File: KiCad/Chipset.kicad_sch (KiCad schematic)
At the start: 9 parts, among them U2 OPTi_82C895, U3 OPTi_82C602, Y1 32768Hz

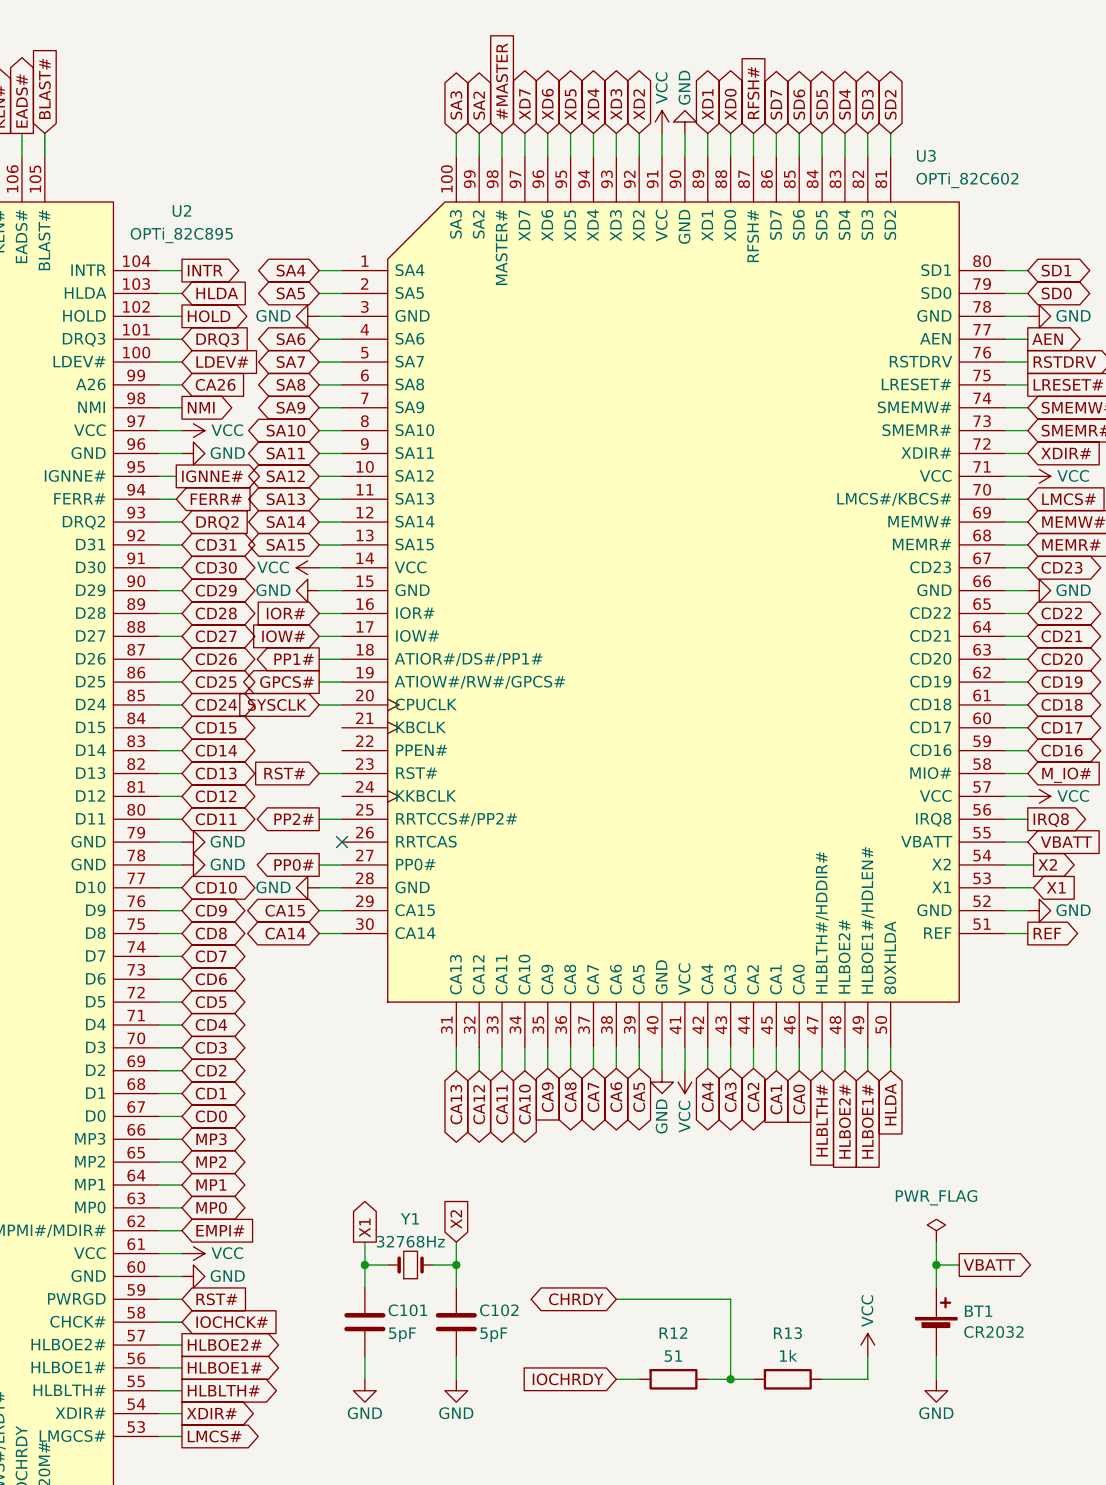
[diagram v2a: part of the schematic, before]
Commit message: Version 0.4: Update chipset connection
Signed-off-by: Sergey Kiselev <skiselev@gmail.com>
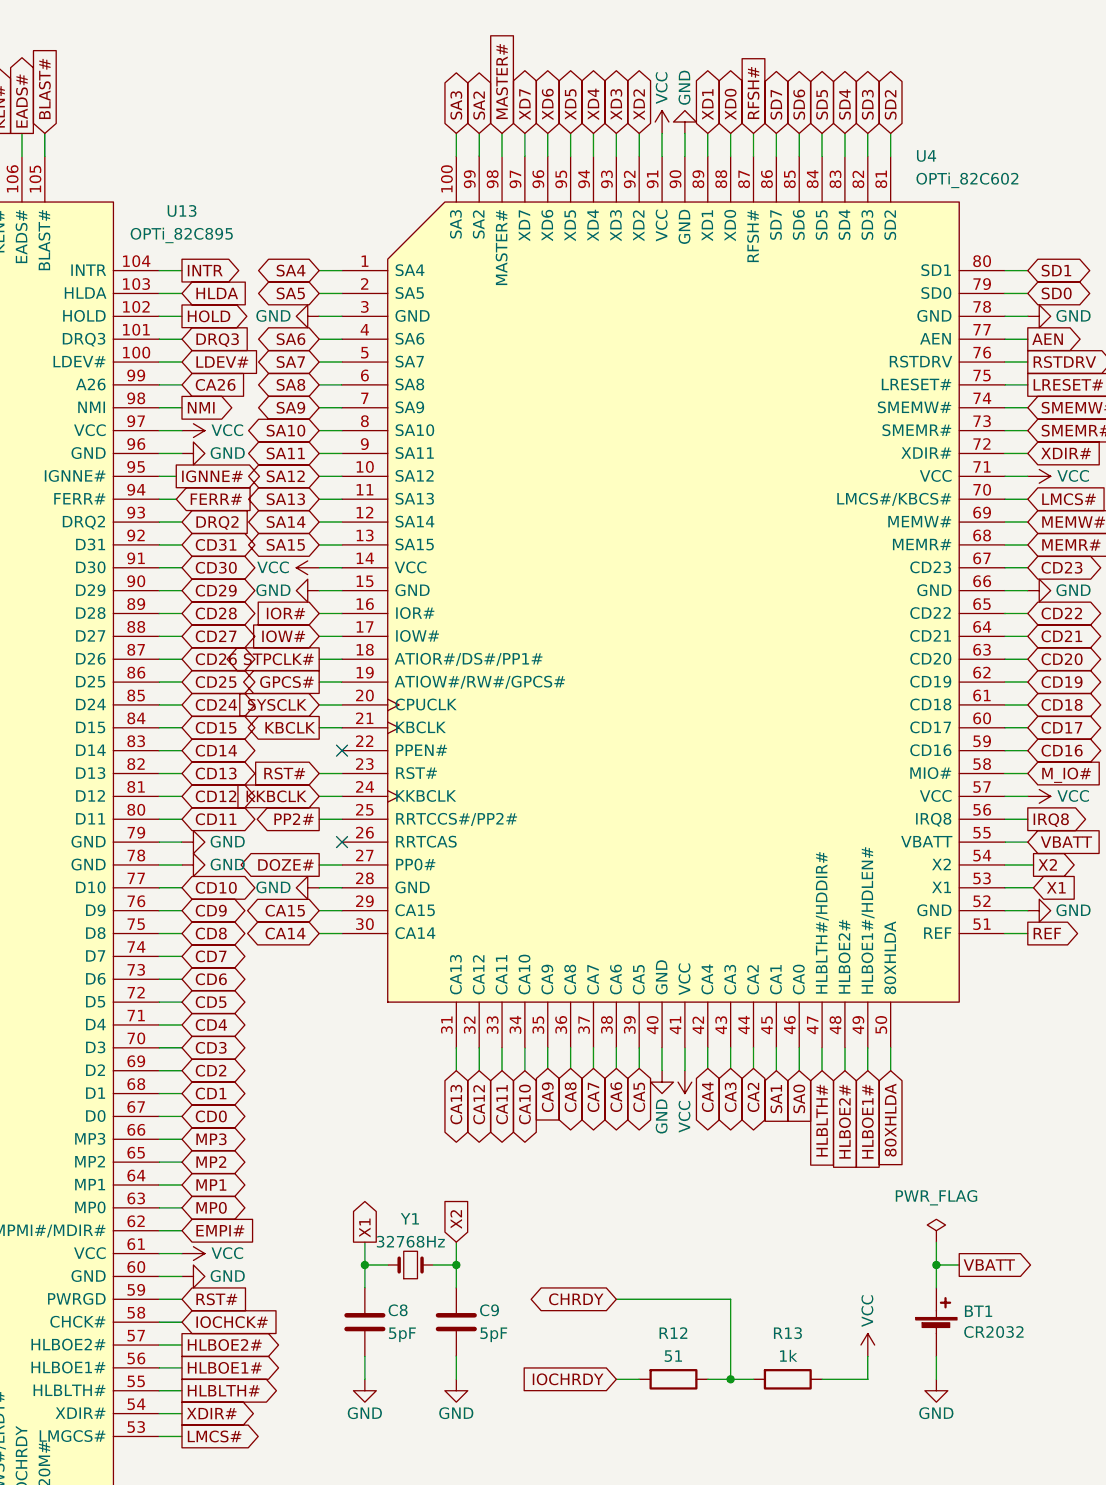
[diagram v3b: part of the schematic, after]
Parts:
- BT1: footprint (none) -> My_Components:Battery_Holder_CR2032_Universal
- C8: renamed from C101; footprint (none) -> Capacitor_SMD:C_0603_1608Metric_Pad1.08x0.95mm_HandSolder
- C9: renamed from C102; footprint (none) -> Capacitor_SMD:C_0603_1608Metric_Pad1.08x0.95mm_HandSolder
- R12, R13, R30: footprint (none) -> Resistor_SMD:R_0612_1632Metric_Pad1.18x3.40mm_HandSolder
- Y1: footprint (none) -> My_Components:Crystal_32K_Horiz
- renumbered U2 to U13, U3 to U4
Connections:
- net CA0 is gone; now on net SA0: U4.46 (CA0)
- net CA1 is gone; now on net SA1: U4.45 (CA1)
- net HLDA: no longer U4.50 (80XHLDA)
- net KBCLK: now reaches U4.21 (KBCLK)
- net KKBCLK: now reaches U4.24 (KKBCLK)
- net #MASTER renamed MASTER#
- net PP0# renamed DOZE#
- net PP1# renamed STPCLK#
- new net 80XHLDA: U4.50 (80XHLDA)
- no-connect marks 2 -> 3
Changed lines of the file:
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@@
   (no_connect (at 200.66 99.06))
   (no_connect (at 25.4 129.54))
+  (no_connect (at 200.66 88.9))
   (wire (pts (xy 167.64 177.8) (xy 167.64 180.34))
     (stroke (width 0) (type default) (color 0 0 0 0))
@@
     (stroke (width 0) (type default) (color 0 0 0 0))
   )
+  (wire (pts (xy 198.12 86.36) (xy 200.66 86.36))
+    (stroke (width 0) (type default) (color 0 0 0 0))
+  )
   (wire (pts (xy 203.2 146.05) (xy 203.2 148.59))
     (stroke (width 0) (type default) (color 0 0 0 0))
@@
     (stroke (width 0) (type default) (color 0 0 0 0))
   )
+  (wire (pts (xy 198.12 93.98) (xy 200.66 93.98))
+    (stroke (width 0) (type default) (color 0 0 0 0))
+  )
   (wire (pts (xy 73.66 180.34) (xy 73.66 177.8))
     (stroke (width 0) (type default) (color 0 0 0 0))
@@
     )
   )
-  (global_label "HLDA" (shape input) (at 261.62 124.46 270) (fields_autoplaced)
+  (global_label "80XHLDA" (shape input) (at 261.62 124.46 270) (fields_autoplaced)
     (effects (font (size 1.27 1.27)) (justify right))
-    (property "Intersheet References" "${INTERSHEET_REFS}" (id 0) (at 261.5406 131.5013 90)
+    (property "Intersheet References" "${INTERSHEET_REFS}" (id 0) (at 261.5406 135.1299 90)
       (effects (font (size 1.27 1.27)) (justify right) hide)
     )
@@
     )
   )
+  (global_label "KBCLK" (shape output) (at 198.12 86.36 180) (fields_autoplaced)
+    (effects (font (size 1.27 1.27)) (justify right))
+    (property "Intersheet References" "${INTERSHEET_REFS}" (id 0) (at 189.6877 86.2806 0)
+      (effects (font (size 1.27 1.27)) (justify right) hide)
+    )
+  )
   (global_label "XD3" (shape bidirectional) (at 231.14 20.32 90) (fields_autoplaced)
     (effects (font (size 1.27 1.27)) (justify left))
@@
     )
   )
-  (global_label "#MASTER" (shape input) (at 218.44 20.32 90) (fields_autoplaced)
+  (global_label "MASTER#" (shape input) (at 218.44 20.32 90) (fields_autoplaced)
     (effects (font (size 1.27 1.27)) (justify left))
     (property "Intersheet References" "${INTERSHEET_REFS}" (id 0) (at 218.3606 9.5896 90)
@@
     )
   )
-  (global_label "PP0#" (shape output) (at 198.12 101.6 180) (fields_autoplaced)
+  (global_label "DOZE#" (shape output) (at 198.12 101.6 180) (fields_autoplaced)
     (effects (font (size 1.27 1.27)) (justify right))
-    (property "Intersheet References" "${INTERSHEET_REFS}" (id 0) (at 190.7763 101.5206 0)
+    (property "Intersheet References" "${INTERSHEET_REFS}" (id 0) (at 189.5668 101.5206 0)
       (effects (font (size 1.27 1.27)) (justify right) hide)
     )
@@
     )
   )
+  (global_label "KKBCLK" (shape input) (at 198.12 93.98 180) (fields_autoplaced)
+    (effects (font (size 1.27 1.27)) (justify right))
+    (property "Intersheet References" "${INTERSHEET_REFS}" (id 0) (at 188.4177 93.9006 0)
+      (effects (font (size 1.27 1.27)) (justify right) hide)
+    )
+  )
   (global_label "SA13" (shape bidirectional) (at 198.12 60.96 180) (fields_autoplaced)
     (effects (font (size 1.27 1.27)) (justify right))
@@
     )
   )
-  (global_label "CA0" (shape input) (at 251.46 124.46 270) (fields_autoplaced)
+  (global_label "SA0" (shape input) (at 251.46 124.46 270) (fields_autoplaced)
     (effects (font (size 1.27 1.27)) (justify right))
-    (property "Intersheet References" "${INTERSHEET_REFS}" (id 0) (at 251.3806 130.3523 90)
+    (property "Intersheet References" "${INTERSHEET_REFS}" (id 0) (at 251.3806 130.2918 90)
       (effects (font (size 1.27 1.27)) (justify right) hide)
     )
@@
     )
   )
-  (global_label "CA1" (shape input) (at 248.92 124.46 270) (fields_autoplaced)
+  (global_label "SA1" (shape input) (at 248.92 124.46 270) (fields_autoplaced)
     (effects (font (size 1.27 1.27)) (justify right))
-    (property "Intersheet References" "${INTERSHEET_REFS}" (id 0) (at 248.8406 130.3523 90)
+    (property "Intersheet References" "${INTERSHEET_REFS}" (id 0) (at 248.8406 130.2918 90)
       (effects (font (size 1.27 1.27)) (justify right) hide)
     )
@@
     )
   )
-  (global_label "PP1#" (shape output) (at 198.12 78.74 180) (fields_autoplaced)
+  (global_label "STPCLK#" (shape output) (at 198.12 78.74 180) (fields_autoplaced)
     (effects (font (size 1.27 1.27)) (justify right))
-    (property "Intersheet References" "${INTERSHEET_REFS}" (id 0) (at 190.7763 78.6606 0)
+    (property "Intersheet References" "${INTERSHEET_REFS}" (id 0) (at 187.5106 78.6606 0)
       (effects (font (size 1.27 1.27)) (justify right) hide)
     )
@@
     (property "Reference" "R12" (id 0) (at 237.49 153.67 90))
     (property "Value" "51" (id 1) (at 237.49 156.21 90))
-    (property "Footprint" "" (id 2) (at 237.49 156.972 90)
+    (property "Footprint" "Resistor_SMD:R_0612_1632Metric_Pad1.18x3.40mm_HandSolder" (id 2) (at 237.49 156.972 90)
       (effects (font (size 1.27 1.27)) hide)
     )
@@
     (property "Reference" "R13" (id 0) (at 250.19 153.67 90))
     (property "Value" "1k" (id 1) (at 250.19 156.21 90))
-    (property "Footprint" "" (id 2) (at 250.19 156.972 90)
+    (property "Footprint" "Resistor_SMD:R_0612_1632Metric_Pad1.18x3.40mm_HandSolder" (id 2) (at 250.19 156.972 90)
       (effects (font (size 1.27 1.27)) hide)
     )
@@
     (property "Reference" "Y1" (id 0) (at 208.28 140.97 0))
     (property "Value" "32768Hz" (id 1) (at 208.28 143.51 0))
-    (property "Footprint" "" (id 2) (at 208.28 146.05 0)
+    (property "Footprint" "My_Components:Crystal_32K_Horiz" (id 2) (at 208.28 146.05 0)
       (effects (font (size 1.27 1.27)) hide)
     )
@@
       (effects (font (size 1.27 1.27)) (justify left))
     )
-    (property "Footprint" "" (id 2) (at 266.7 152.146 90)
+    (property "Footprint" "My_Components:Battery_Holder_CR2032_Universal" (id 2) (at 266.7 152.146 90)
       (effects (font (size 1.27 1.27)) hide)
     )
@@
     (property "Reference" "R30" (id 0) (at 62.23 190.5 90))
     (property "Value" "33" (id 1) (at 62.23 193.04 90))
-    (property "Footprint" "" (id 2) (at 62.23 193.802 90)
+    (property "Footprint" "Resistor_SMD:R_0612_1632Metric_Pad1.18x3.40mm_HandSolder" (id 2) (at 62.23 193.802 90)
       (effects (font (size 1.27 1.27)) hide)
     )
@@
   (symbol (lib_id "Device:C") (at 213.36 152.4 0) (unit 1)
     (in_bom yes) (on_board yes)
-    (property "Reference" "C102" (id 0) (at 215.9 151.13 0)
+    (property "Reference" "C9" (id 0) (at 215.9 151.13 0)
       (effects (font (size 1.27 1.27)) (justify left))
     )
@@
       (effects (font (size 1.27 1.27)) (justify left))
     )
-    (property "Footprint" "" (id 2) (at 214.3252 156.21 0)
+    (property "Footprint" "Capacitor_SMD:C_0603_1608Metric_Pad1.08x0.95mm_HandSolder" (id 2) (at 214.3252 156.21 0)
       (effects (font (size 1.27 1.27)) hide)
     )
@@
   (symbol (lib_id "my_components:OPTi_82C602") (at 237.49 72.39 270) (unit 1)
     (in_bom yes) (on_board yes) (fields_autoplaced)
-    (property "Reference" "U3" (id 0) (at 264.3887 22.86 90)
+    (property "Reference" "U4" (id 0) (at 264.3887 22.86 90)
       (effects (font (size 1.27 1.27)) (justify left))
     )
@@
   (symbol (lib_id "my_components:OPTi_82C895") (at 102.87 100.33 0) (unit 1)
     (in_bom yes) (on_board yes) (fields_autoplaced)
-    (property "Reference" "U2" (id 0) (at 182.88 28.9812 0))
+    (property "Reference" "U13" (id 0) (at 182.88 28.9812 0))
     (property "Value" "OPTi_82C895" (id 1) (at 182.88 31.5212 0))
     (property "Footprint" "Package_QFP:PQFP-208_28x28mm_P0.5mm" (id 2) (at 102.87 107.95 0)
@@
   (symbol (lib_id "Device:C") (at 203.2 152.4 0) (unit 1)
     (in_bom yes) (on_board yes)
-    (property "Reference" "C101" (id 0) (at 205.74 151.13 0)
+    (property "Reference" "C8" (id 0) (at 205.74 151.13 0)
       (effects (font (size 1.27 1.27)) (justify left))
     )
@@
       (effects (font (size 1.27 1.27)) (justify left))
     )
-    (property "Footprint" "" (id 2) (at 204.1652 156.21 0)
+    (property "Footprint" "Capacitor_SMD:C_0603_1608Metric_Pad1.08x0.95mm_HandSolder" (id 2) (at 204.1652 156.21 0)
       (effects (font (size 1.27 1.27)) hide)
     )
